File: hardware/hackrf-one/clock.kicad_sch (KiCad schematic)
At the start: 67 parts, among them P1 AD_CLK, P16 CLKIN, P2 CLKOUT, P21 MIX_CLK, P37 SCL, P38 SDA, P57 XCVR_CLK, P59 GCK2, P60 SGPIO_CLK, P72 GP_CLKIN, P8 FSX2_CLK, U16 74LVC1G3157, U19 Si5351A-B-GT, U22 74LVC1G80, U26 74AUP2G58GU, U27 74AUP2G58GU, U28 74AUP2G58GU, U29 74AUP2G58GU, X1 MAIN_XTAL

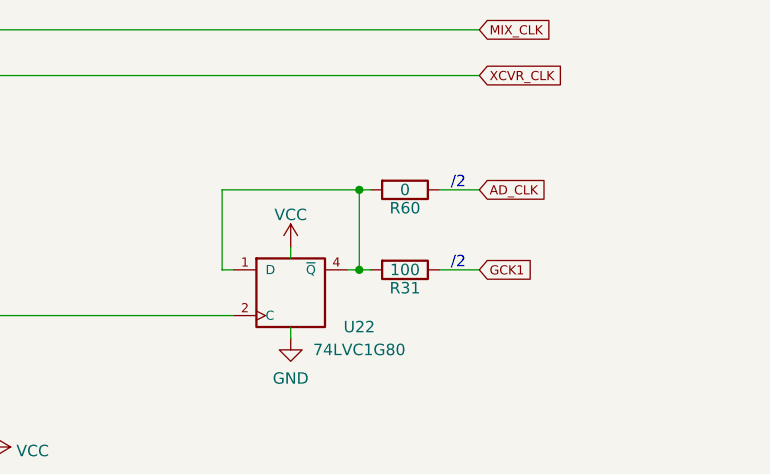
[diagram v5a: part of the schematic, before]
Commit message: HackRF One: change R60 from 0 ohms to 100 ohms
This matches R31 and was intended to be done when R31 was changed to 100
ohms.
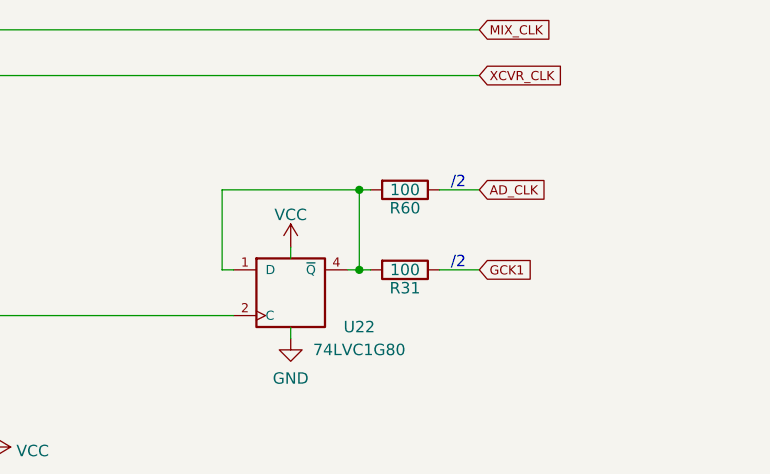
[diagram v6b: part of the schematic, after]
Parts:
- R60: value 0 -> 100; Manufacturer Stackpole -> Yageo; Part Number RMCF0402ZT0R00 -> RC0402JR-07100RL
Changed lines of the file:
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@@
     (in_bom yes) (on_board yes)
     (property "Reference" "R60" (id 0) (at 366.395 47.117 90))
-    (property "Value" "0" (id 1) (at 366.395 45.085 90))
+    (property "Value" "100" (id 1) (at 366.395 45.085 90))
     (property "Footprint" "hackrf:GSG-0402" (id 2) (at 366.395 45.085 0)
       (effects (font (size 1.524 1.524)) hide)
@@
       (effects (font (size 1.524 1.524)) hide)
     )
-    (property "Manufacturer" "Stackpole" (id 4) (at 366.395 45.085 0)
+    (property "Manufacturer" "Yageo" (id 4) (at 366.395 45.085 0)
       (effects (font (size 1.524 1.524)) hide)
     )
-    (property "Part Number" "RMCF0402ZT0R00" (id 5) (at 366.395 45.085 0)
+    (property "Part Number" "RC0402JR-07100RL" (id 5) (at 366.395 45.085 0)
       (effects (font (size 1.524 1.524)) hide)
     )
-    (property "Description" "RES 0.0 OHM 1/16W 0402 SMD" (id 6) (at 366.395 45.085 0)
+    (property "Description" "RES 100 OHM 5% 1/16W 0402" (id 6) (at 366.395 45.085 0)
       (effects (font (size 1.524 1.524)) hide)
     )
